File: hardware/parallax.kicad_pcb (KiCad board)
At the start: 2 copper layers, 89.9 x 52.3 mm, 102 parts, among them J1 Conn_Coaxial, J2 Conn_Coaxial, J3 Conn_Coaxial, J4 Conn_01x10_Pin, J5 Conn_01x02_Pin, J6 Conn_01x02_Pin, J7 Conn_01x02_Pin, SW2 SW_Push, U1 Pico, U2 MCP6002-xMC, U3 4052, U4 MCP6002-xMC, U5 4052, U6 sgm8301

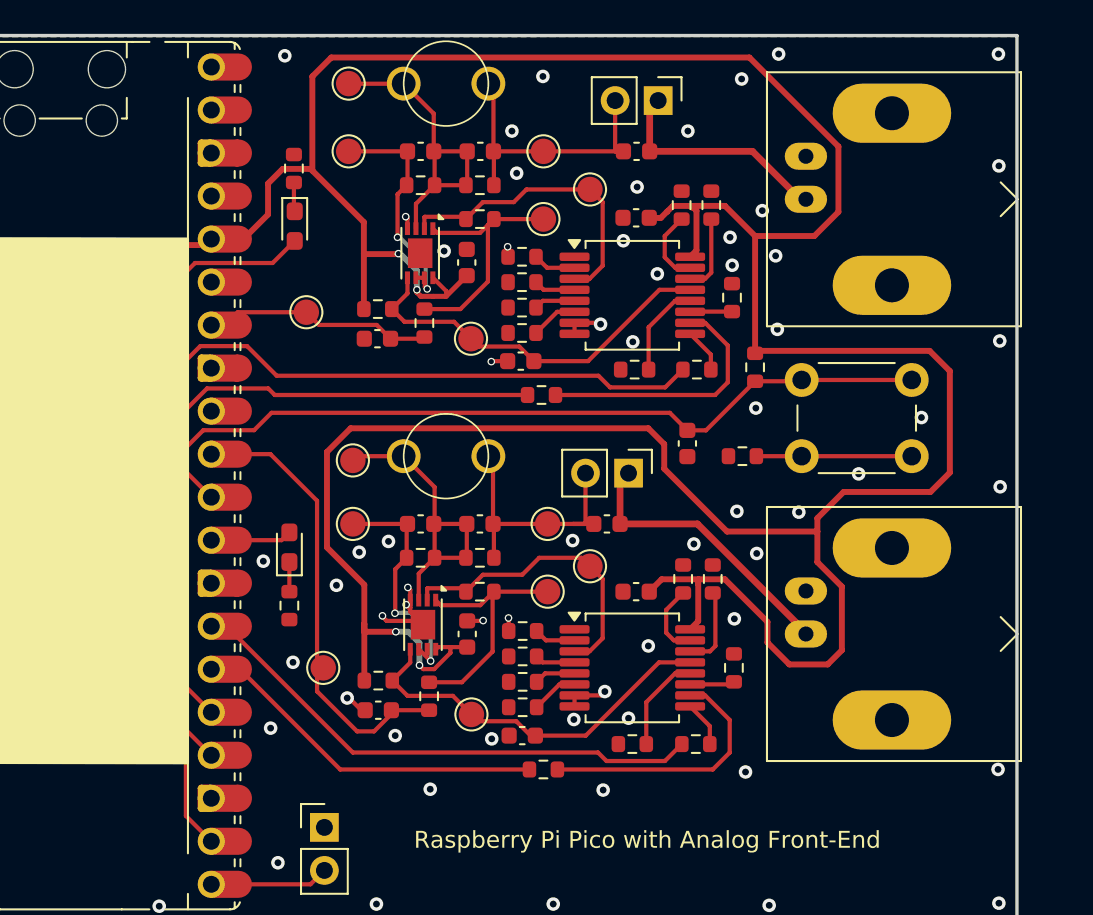
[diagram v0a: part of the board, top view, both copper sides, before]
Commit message: Update Trimmer Capacitor Footprint
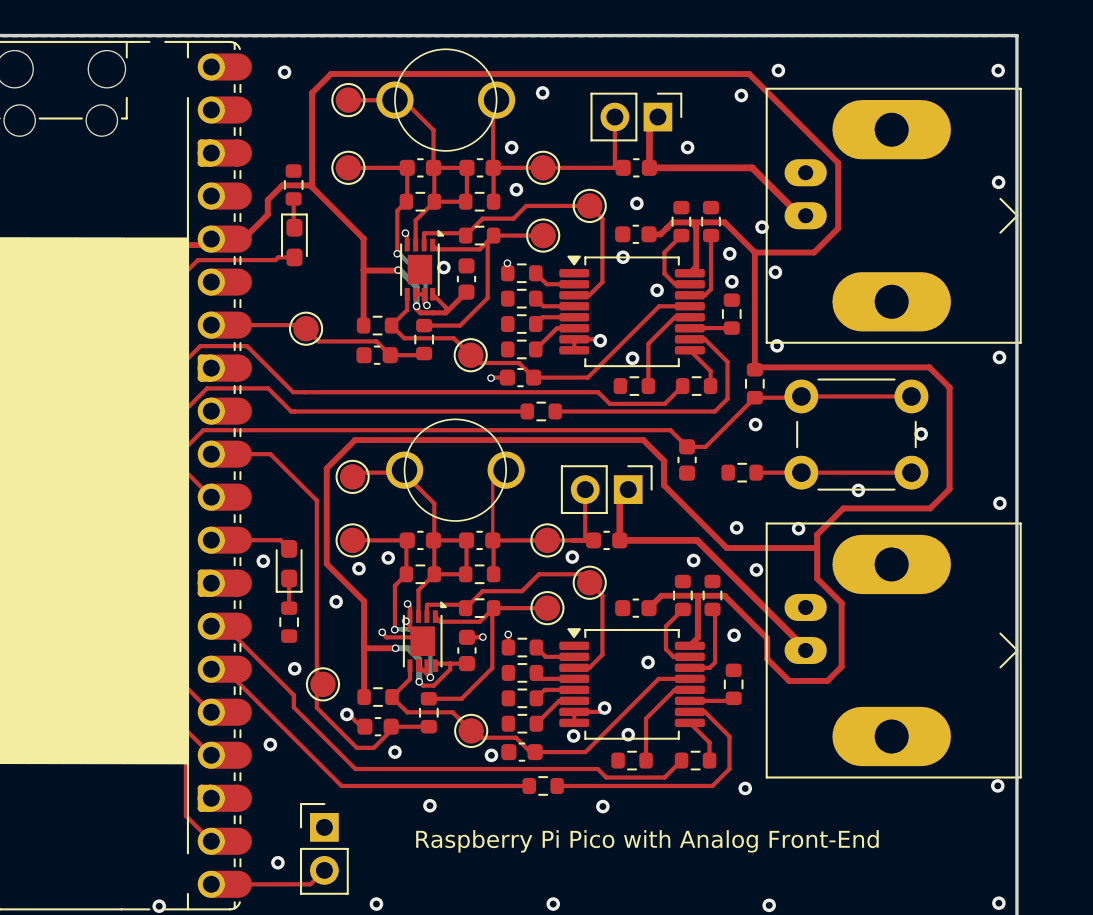
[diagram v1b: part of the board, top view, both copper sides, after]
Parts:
- moved C4 0.99 mm to (185.0, 55.1)
- moved C17 0.97 mm to (185.7, 43.8)
- moved R20 0.97 mm to (180.5, 46.5)
- moved R27 0.97 mm to (189.0, 46.4)
- moved R28 0.97 mm to (189.0, 43.4)
- moved R29 0.97 mm to (189.0, 44.9)
- moved R30 0.97 mm to (189.0, 47.9)
- moved R34 0.97 mm to (183.2, 47.4)
- moved TP10 0.97 mm to (186.0, 48.3)
- moved U4 0.97 mm to (183.0, 43.2)
- moved C1 0.97 mm to (198.7, 54.5)
- moved C10 0.97 mm to (188.9, 49.6)
- moved C11 0.97 mm to (195.7, 37.2)
- moved C12 0.97 mm to (184.5, 33.2)
- moved C13 0.97 mm to (186.5, 37.2)
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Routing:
- net MUL_1A: track 20.4 -> 21.7 mm
- net /Analog Front-End/ADC: track 26.1 -> 27.0 mm
- net MUL_1B: track 30.7 -> 31.6 mm
- net +3V3: track 259.5 -> 258.7 mm

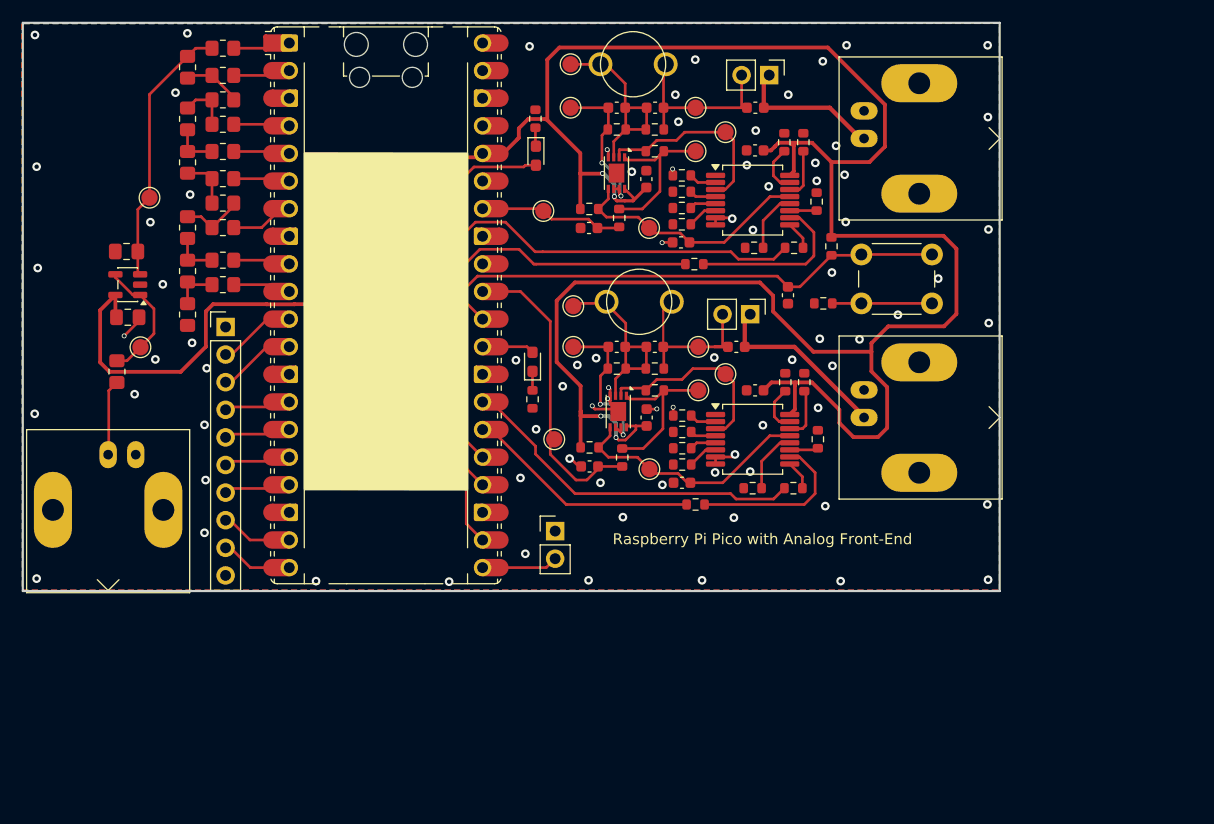
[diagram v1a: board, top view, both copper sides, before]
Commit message: reduced length of reference channel by 6mm
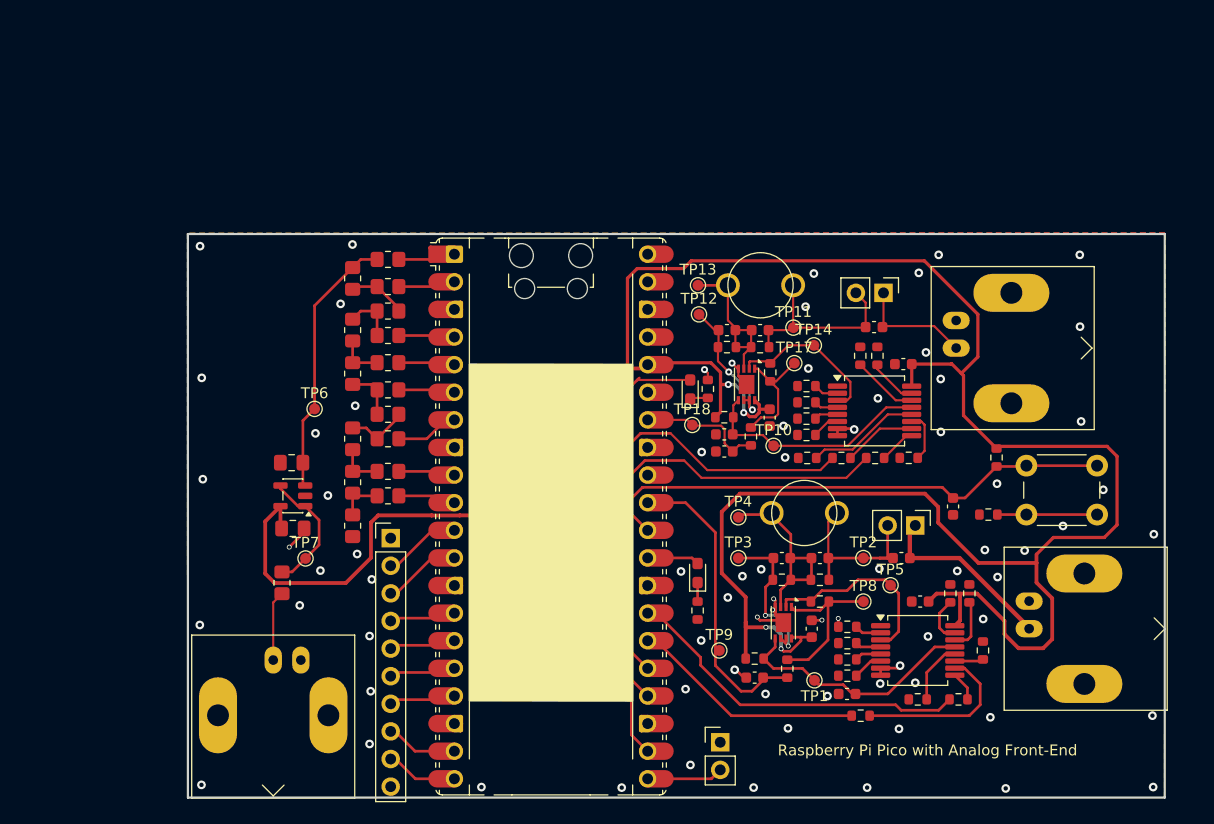
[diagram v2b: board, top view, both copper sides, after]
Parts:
- TP1, TP10, TP11, TP12, TP13, TP14, TP17, TP18, TP2, TP3, TP4, TP5, TP6, TP7, TP8, TP9: footprint TestPoint:TestPoint_Pad_D1.5mm -> TestPoint:TestPoint_Pad_D1.0mm
- moved R2 29.5 mm to (191.4, 63.1)
- moved D2 25.8 mm to (189.7, 63.1), turned to 90 degrees
- moved R26 25.0 mm to (209.8, 69.4), turned to 180 degrees
- moved C17 24.7 mm to (197.1, 65.7), turned to -90 degrees
- moved C18 24.7 mm to (153.1, 69.9)
- moved J5 24.7 mm to (192.5, 95.6)
- moved TP7 24.7 mm to (154.4, 78.7)
- moved R35 24.7 mm to (161.9, 51.2)
- moved R36 24.7 mm to (161.9, 53.7)
- moved R37 24.7 mm to (161.9, 58.2)
- moved R38 24.7 mm to (161.9, 60.7)
- moved R39 24.7 mm to (161.9, 63.2)
- moved R44 24.7 mm to (158.7, 52.9)
- moved R45 24.7 mm to (161.9, 55.9)
- moved R46 24.7 mm to (158.7, 57.7)
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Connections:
- U1 pad 24: MUL_2B -> MUL_2A
- U1 pad 25: MUL_2A -> MUL_2B
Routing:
- net MUL_2B: track 57.8 -> 42.6 mm
- net +3V3: track 258.7 -> 248.8 mm
- net Net-(U5-A): track 15.4 -> 6.75 mm
- net MUL_2A: track 40.3 -> 47.1 mm
- net Net-(U5-X0): track 5.60 -> 10.4 mm
- net Net-(R33-Pad1): track 15.2 -> 11.1 mm
- net Net-(U4A--): track 18.0 -> 14.8 mm
- net Net-(U4A-+): track 18.9 -> 16.0 mm
- net /Analog Front-End1/analog_in: track 13.6 -> 10.7 mm
- net Net-(J7-Pin_2): track 16.4 -> 19.0 mm
- net Net-(U5-X3): track 2.48 -> 4.62 mm
- net /Analog Front-End1/ADC: track 12.5 -> 10.9 mm
- net Net-(U5-X1): track 4.56 -> 6.08 mm
- net GND: track 17.7 -> 19.0 mm, vias 81 -> 75
- net Net-(U4B-+): track 22.9 -> 21.7 mm
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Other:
- board size 89.9 x 52.3 mm -> 89.9 x 51.8 mm

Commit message: reduce afe size by 6mm
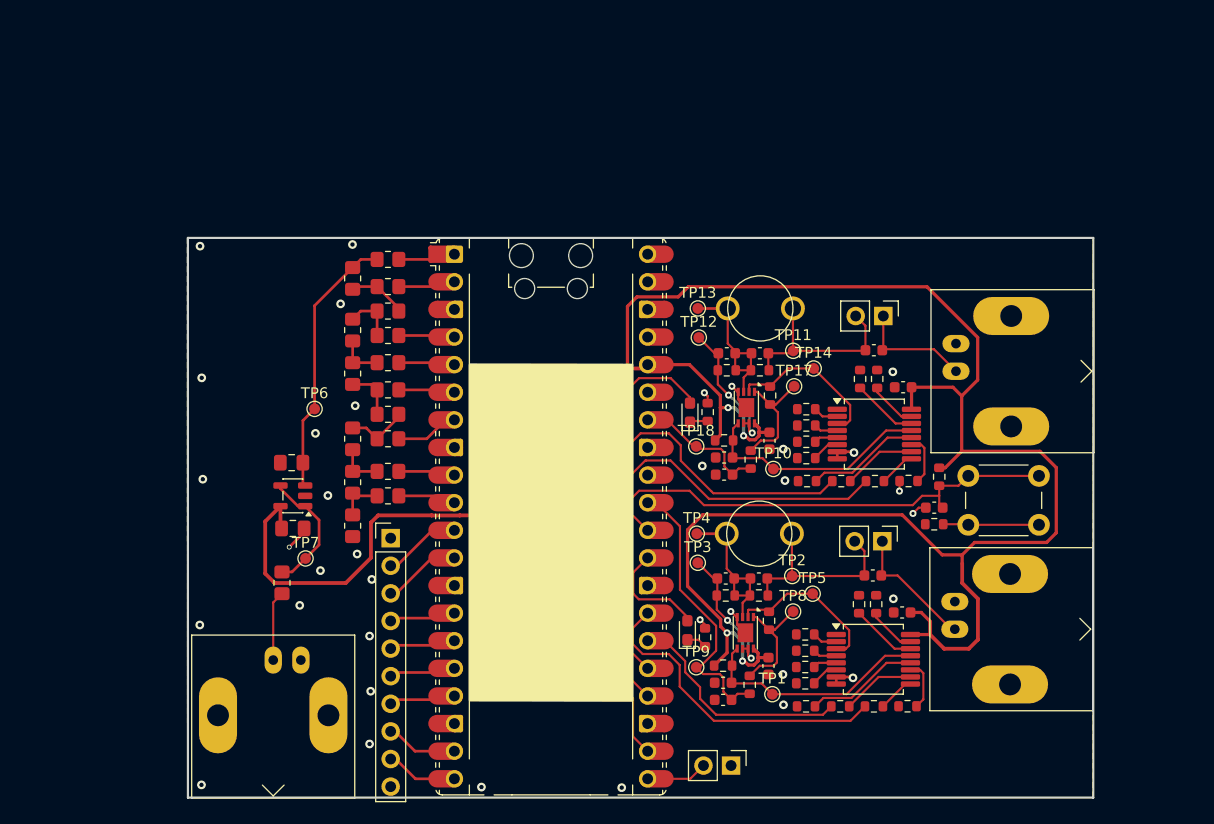
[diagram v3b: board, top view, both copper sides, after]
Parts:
- moved C2 11.4 mm to (192.8, 90.1)
- moved R8 10.3 mm to (200.4, 92.3)
- moved R9 10.2 mm to (205.3, 82.9)
- moved R11 8.63 mm to (209.7, 92.3), turned to 180 degrees
- moved R16 7.80 mm to (206.6, 92.3)
- moved TP5 7.21 mm to (201.0, 81.9)
- moved R10 6.90 mm to (206.8, 82.9)
- moved J1 6.84 mm to (214.1, 85.2)
- moved TP2 6.75 mm to (199.1, 80.3)
- moved TP8 6.53 mm to (199.2, 83.6)
- moved C5 5.92 mm to (196.1, 80.5)
- moved R6 5.80 mm to (196.1, 82.1)
- moved R3 5.56 mm to (212.6, 71.2)
- moved C6 5.49 mm to (193.0, 80.5)
- moved SW2 5.43 mm to (215.3, 71.1)
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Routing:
- net +3V3: track 248.8 -> 229.4 mm
- net Net-(U3-A): track 15.5 -> 6.75 mm
- net LED_1: track 4.01 -> 10.1 mm
- net /Analog Front-End/analog_in: track 16.9 -> 12.1 mm
- net Net-(U3-X0): track 5.77 -> 10.4 mm
- net Net-(R18-Pad1): track 15.1 -> 11.1 mm
- net Reset: track 48.5 -> 44.8 mm
- net Net-(U2A--): track 18.0 -> 14.8 mm
- net Net-(J6-Pin_2): track 16.2 -> 19.0 mm
- net GND: track 19.0 -> 16.2 mm, vias 75 -> 35
- net Net-(U2A-+): track 18.5 -> 16.0 mm
- net MUL_1B: track 31.6 -> 29.5 mm
- net Net-(U3-X3): track 2.65 -> 4.62 mm
- net MUL_2A: track 47.1 -> 48.9 mm
- net /Analog Front-End/ADC: track 27.0 -> 25.5 mm
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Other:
- board size 89.9 x 51.8 mm -> 83.3 x 51.5 mm
- board text removed: "Raspberry Pi Pico with Analog Front-End"
